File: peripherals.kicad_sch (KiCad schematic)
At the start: 0 parts

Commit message: Initiliase main components
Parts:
- added BZ1: Buzzer, Buzzer_Beeper:Buzzer_CUI_CPT-9019S-SMT, symbol Device:Buzzer
- added J10: Cam 2, S05B_PASK_2_LF__SN_:CONN_S05B-PASK-2_JST, symbol 2025-06-21_05-21-07:S05B-PASK-2LFSN
- added J11: Cam 3, S05B_PASK_2_LF__SN_:CONN_S05B-PASK-2_JST, symbol 2025-06-21_05-21-07:S05B-PASK-2LFSN
- added J12: Encoder, Connector_PinHeader_1.00mm:PinHeader_1x04_P1.00mm_Vertical, symbol Connector:Conn_01x04_Pin
- added J13: Servo, Connector_PinHeader_1.00mm:PinHeader_1x03_P1.00mm_Vertical, symbol Connector:Conn_01x03_Pin
- added J9: Cam 1, S05B_PASK_2_LF__SN_:CONN_S05B-PASK-2_JST, symbol 2025-06-21_05-21-07:S05B-PASK-2LFSN

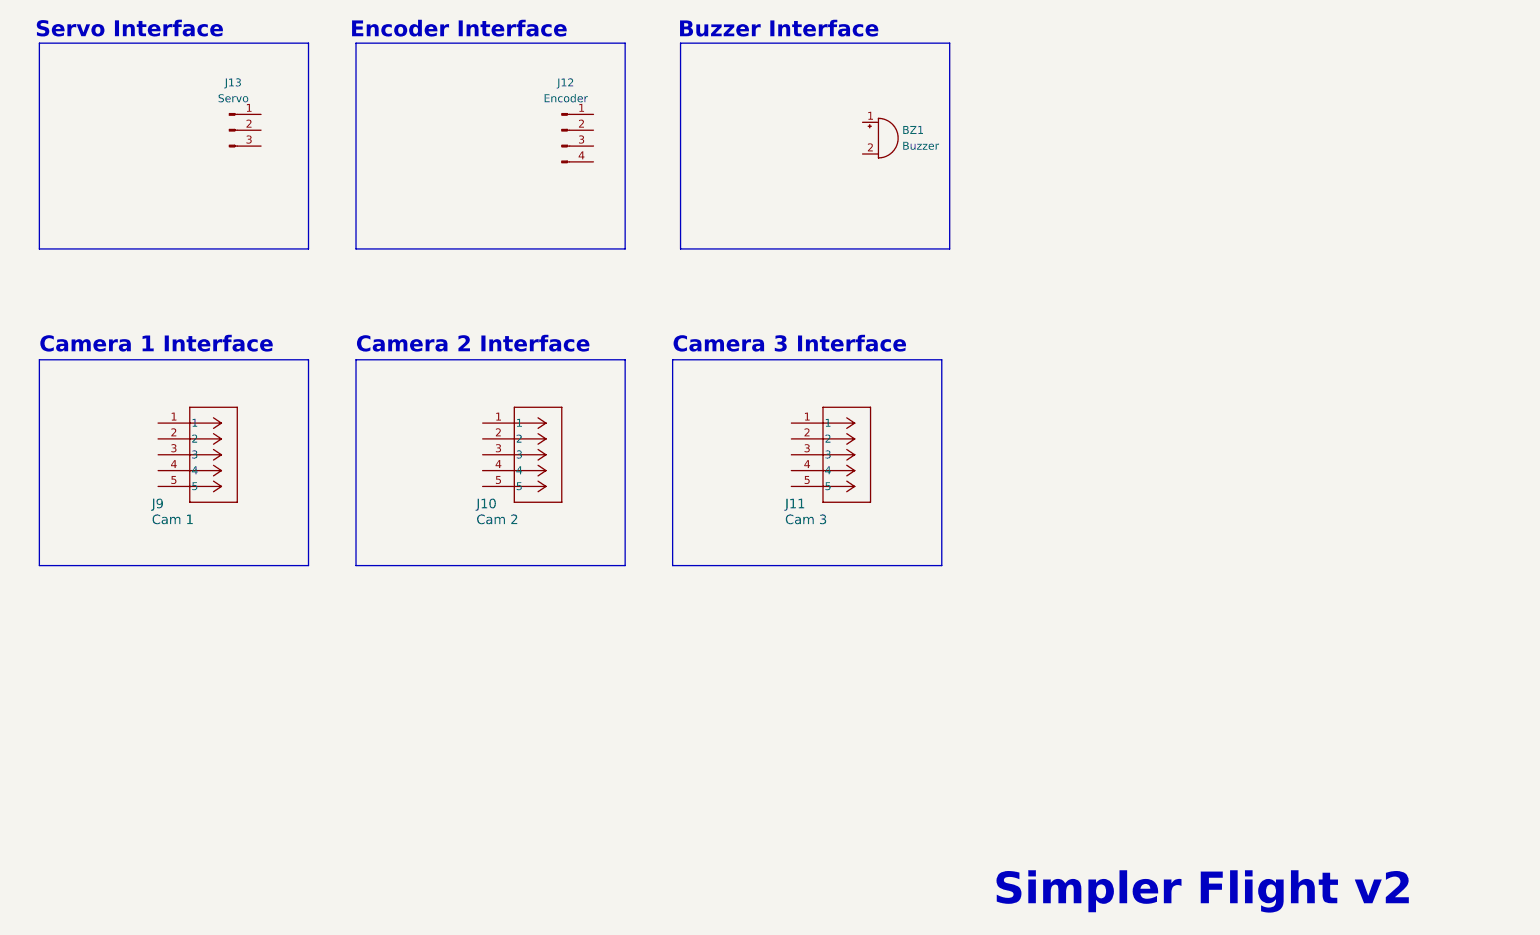
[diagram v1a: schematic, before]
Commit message: Update schematic, pending power sims, updated README
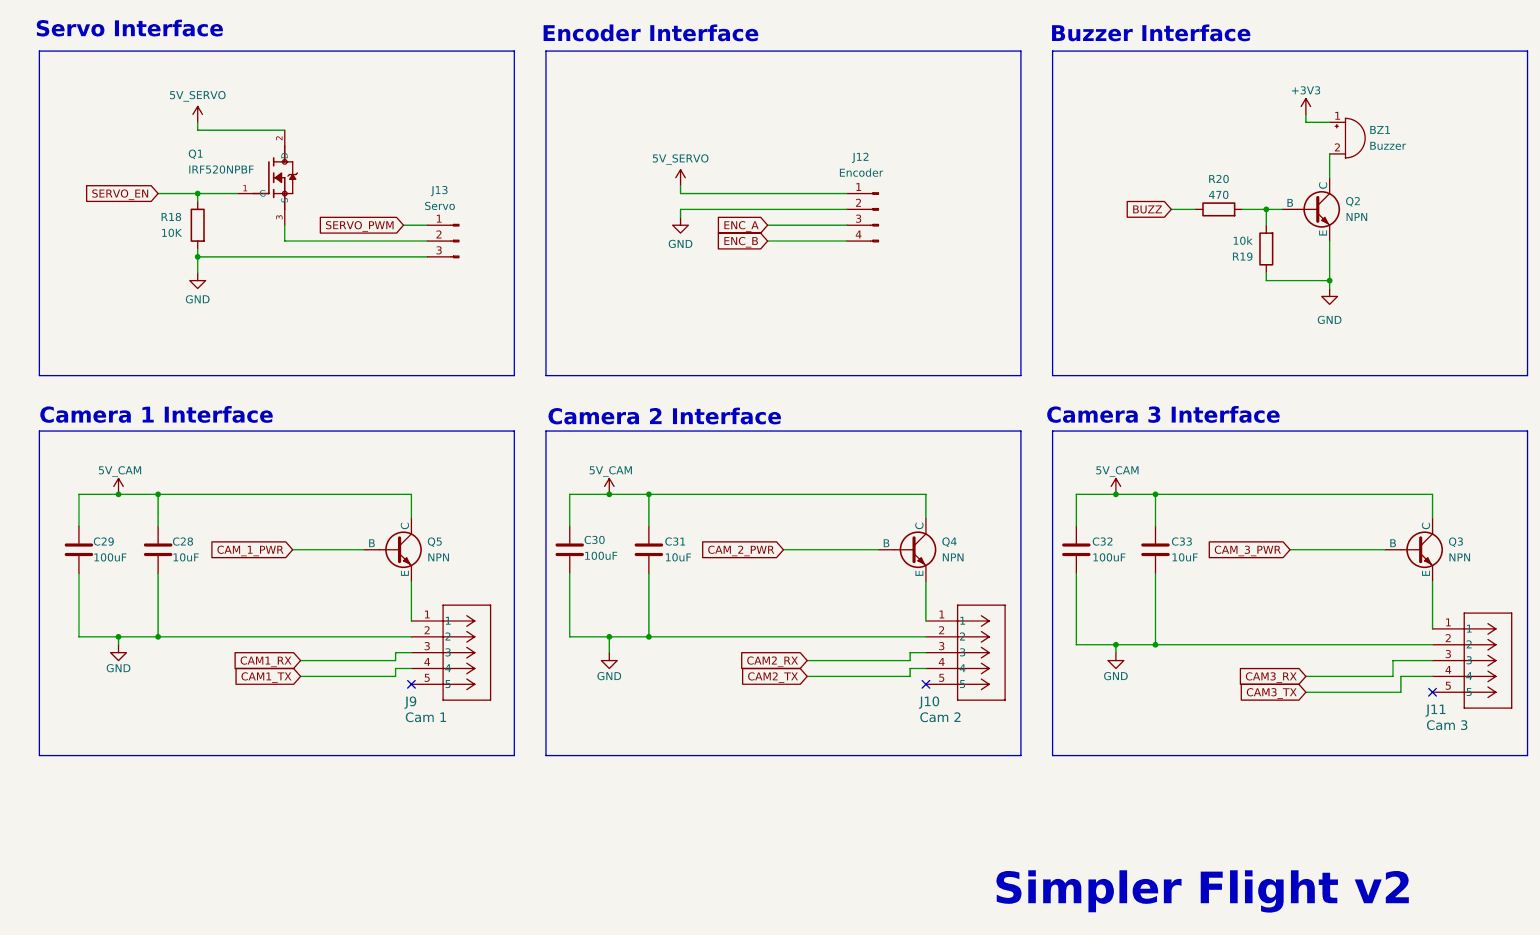
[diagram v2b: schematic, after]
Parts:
- added C28, C31, C33: 10uF, Capacitor_SMD:C_0805_2012Metric_Pad1.18x1.45mm_HandSolder, symbol Device:C
- added C29, C30, C32: 100uF, Capacitor_SMD:C_0805_2012Metric_Pad1.18x1.45mm_HandSolder, symbol Device:C
- added Q1: IRF520NPBF, IRF520NPBF:TO-220-3, symbol IRF520NPBF:IRF520NPBF
- added Q2, Q3, Q4, Q5: NPN, FSB560A:SSOT3_3X1P5_ONS, symbol Simulation_SPICE:NPN
- added R18: 10K, Resistor_SMD:R_0805_2012Metric_Pad1.20x1.40mm_HandSolder, symbol Device:R
- added R19: 10k, Resistor_SMD:R_0805_2012Metric_Pad1.20x1.40mm_HandSolder, symbol Device:R
- added R20: 470, Resistor_SMD:R_0805_2012Metric_Pad1.20x1.40mm_HandSolder, symbol Device:R
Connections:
- net +3V3: now reaches BZ1.1 (+)
- net at BZ1.2 (-): now also Q2.1 (C)
- net at J11.1: now also Q3.3 (E)
- net GND: now reaches J11.2
- net GND: now also J10.2, J12.2 (Pin_2), J13.3 (Pin_3), J9.2, C28.2, C29.2, C30.2, C31.2, C32.2, C33.2, Q2.3 (E), R18.2, R19.1
- net CAM3_RX: now reaches J11.3
- net CAM3_TX: now reaches J11.4
- net at J10.1: now also Q4.3 (E)
- net CAM2_RX: now reaches J10.3
- net CAM2_TX: now reaches J10.4
- net at J9.1: now also Q5.3 (E)
- net CAM1_RX: now reaches J9.3
- net CAM1_TX: now reaches J9.4
- net 5V_SERVO: now reaches J12.1 (Pin_1)
- net 5V_SERVO: now also Q1.2 (D)
- net ENC_A: now reaches J12.3 (Pin_3)
- net ENC_B: now reaches J12.4 (Pin_4)
- net SERVO_PWM: now reaches J13.1 (Pin_1)
- net at J13.2 (Pin_2): now also Q1.3 (S)
- new net: Q2.2 (B), R19.2, R20.2
- new net 5V_CAM: C28.1, C29.1, C30.1, C31.1, C32.1, C33.1, Q3.1 (C), Q4.1 (C), Q5.1 (C)
- new net BUZZ: R20.1
- new net CAM_1_PWR: Q5.2 (B)
- new net CAM_2_PWR: Q4.2 (B)
- new net CAM_3_PWR: Q3.2 (B)
- new net SERVO_EN: Q1.1 (G), R18.1
- no-connect marks 0 -> 3
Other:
- moved on the sheet: BZ1, J10, J11, J12, J13, J9

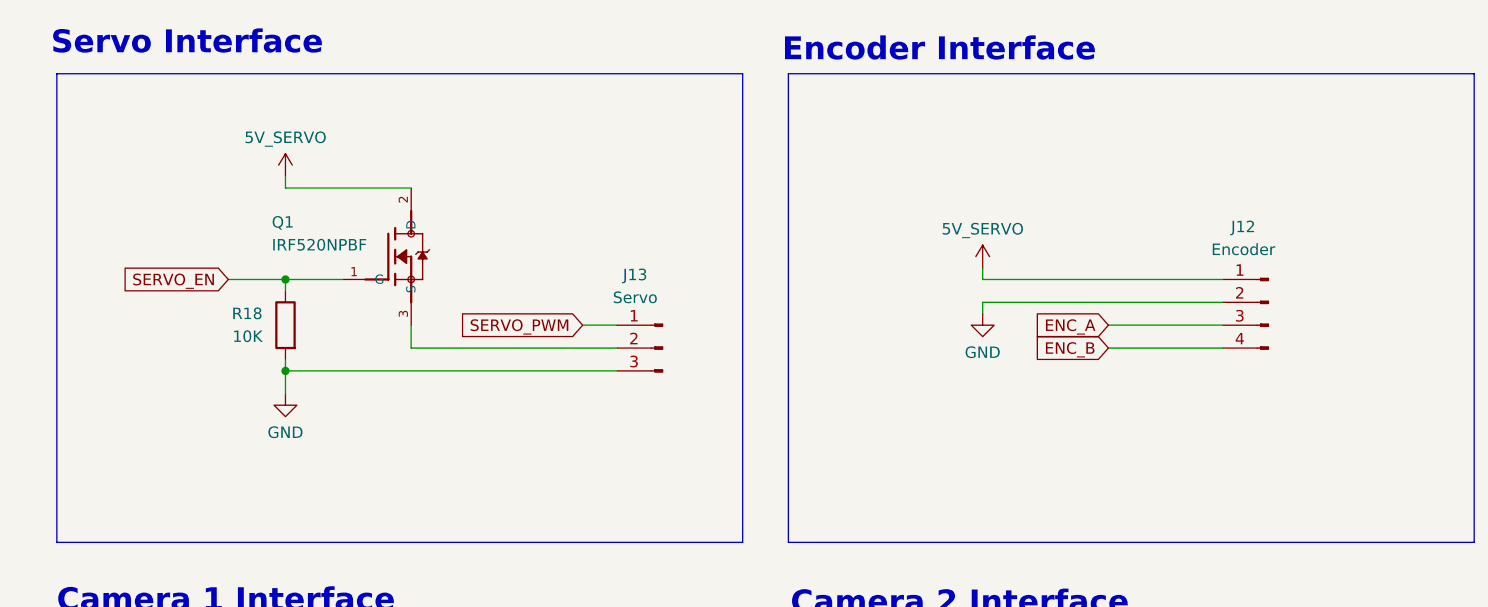
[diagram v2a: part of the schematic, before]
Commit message: Remove transistor enable for servo power. Added falstad sim files
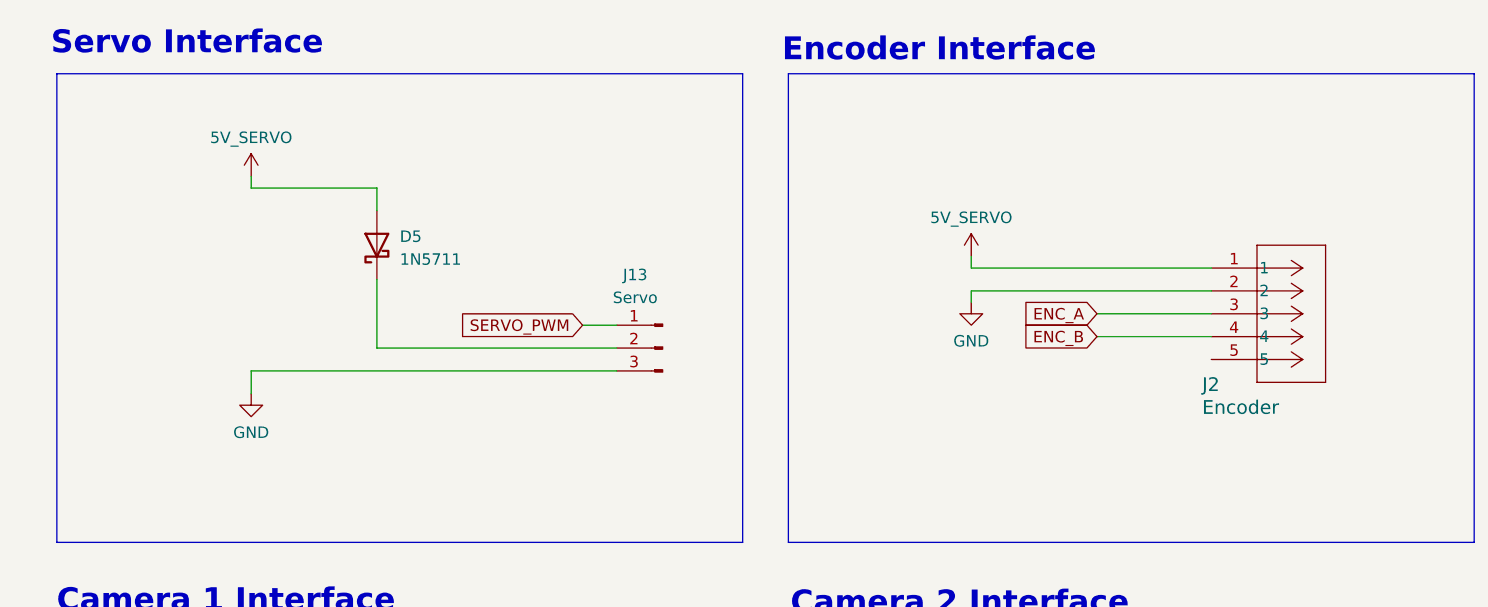
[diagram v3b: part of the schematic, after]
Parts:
- removed J12: Encoder, Connector_PinHeader_1.00mm:PinHeader_1x04_P1.00mm_Vertical, symbol Connector:Conn_01x04_Pin
- removed Q1: IRF520NPBF, IRF520NPBF:TO-220-3, symbol IRF520NPBF:IRF520NPBF
- removed R18: 10K, Resistor_SMD:R_0805_2012Metric_Pad1.20x1.40mm_HandSolder, symbol Device:R
- added D5: 1N5711, Diode_THT:D_DO-35_SOD27_P7.62mm_Horizontal, symbol Diode:1N5711
- added J2: Encoder, S05B_PASK_2_LF__SN_:CONN_S05B-PASK-2_JST, symbol 2025-06-21_05-21-07:S05B-PASK-2LFSN
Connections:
- net 5V_SERVO: now also D5.2 (A), J2.1
- net ENC_A: now also J2.3
- net ENC_B: now also J2.4
- net GND: now also J2.2
- net at J13.2 (Pin_2): now also D5.1 (K)

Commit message: Updated schematics
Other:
- note added: "CAS Board 2025"
- note removed: "Simpler Flight v2"

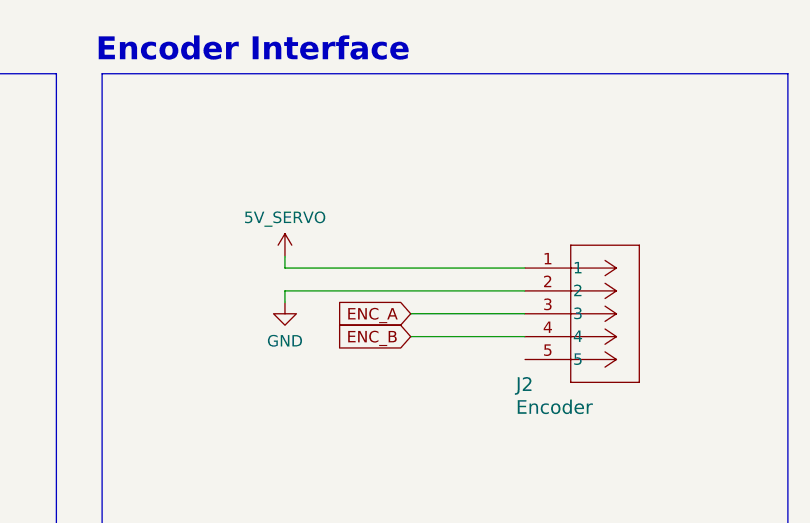
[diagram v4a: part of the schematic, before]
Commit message: added schotkey diode for encoder power
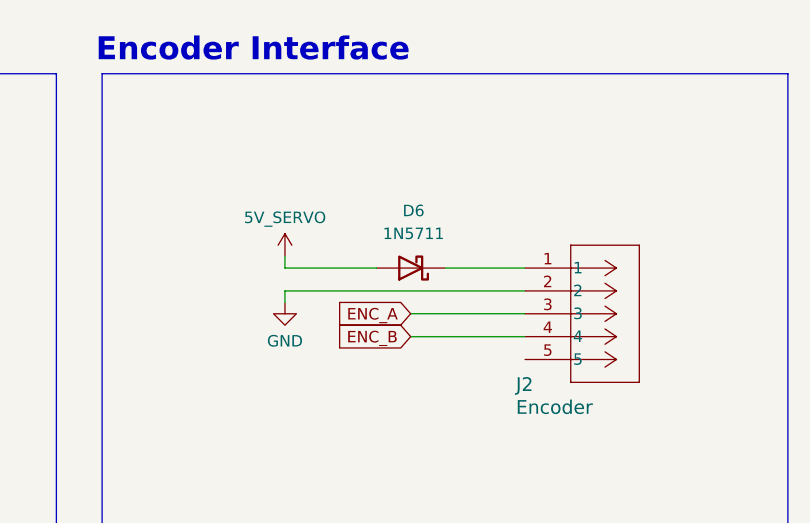
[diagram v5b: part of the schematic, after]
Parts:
- added D6: 1N5711, Diode_THT:D_DO-35_SOD27_P7.62mm_Horizontal, symbol Diode:1N5711
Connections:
- net 5V_SERVO: now also D6.2 (A); no longer J2.1
- new net: D6.1 (K), J2.1
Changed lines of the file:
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@@
 	(wire
 		(pts
+			(xy 144.78 60.96) (xy 153.67 60.96)
+		)
+		(stroke
+			(width 0)
+			(type default)
+		)
+	)
+	(wire
+		(pts
 			(xy 82.55 139.7) (xy 82.55 138.43)
 		)
@@
 	(wire
 		(pts
+			(xy 127 60.96) (xy 137.16 60.96)
+		)
+		(stroke
+			(width 0)
+			(type default)
+		)
+	)
+	(wire
+		(pts
 			(xy 85.09 124.46) (xy 85.09 130.81)
 		)
@@
 		)
 	)
-	(wire
-		(pts
-			(xy 153.67 60.96) (xy 127 60.96)
-		)
-		(stroke
-			(width 0)
-			(type default)
-		)
-	)
 	(polyline
 		(pts
@@
 					(unit 1)
 				)
+			)
+		)
+	)
+	(symbol
+		(lib_id "Diode:1N5711")
+		(at 140.97 60.96 180)
+		(unit 1)
+		(exclude_from_sim no)
+		(in_bom yes)
+		(on_board yes)
+		(dnp no)
+		(fields_autoplaced yes)
+		(property "Reference" "D6"
+			(at 141.2875 54.61 0)
+			(effects
+				(font
+					(size 1.27 1.27)
+				)
+			)
+		)
+		(property "Value" "1N5711"
+			(at 141.2875 57.15 0)
+			(effects
+				(font
+					(size 1.27 1.27)
+				)
+			)
+		)
+		(property "Footprint" "Diode_THT:D_DO-35_SOD27_P7.62mm_Horizontal"
+			(at 140.97 56.515 0)
+			(effects
+				(font
+					(size 1.27 1.27)
+				)
+				(hide yes)
+			)
+		)
+		(property "Datasheet" "https://www.microsemi.com/document-portal/doc_download/8865-lds-0040-datasheet"
+			(at 140.97 60.96 0)
+			(effects
+				(font
+					(size 1.27 1.27)
+				)
+				(hide yes)
+			)
+		)
+		(property "Description" "70V 33mA Schottky diode, DO-35"
+			(at 140.97 60.96 0)
+			(effects
+				(font
+					(size 1.27 1.27)
+				)
+				(hide yes)
+			)
+		)
+		(pin "2"
+		)
+		(pin "1"
+		)
+		(instances
+			(project "SimplerFlight_v2"
+				(path "/05521696-5bcb-4d0e-9e87-bbc993e58ce4/48646a32-6556-4772-9e6c-3c45575ecce9"
+					(reference "D6")
+					(unit 1)
+				)

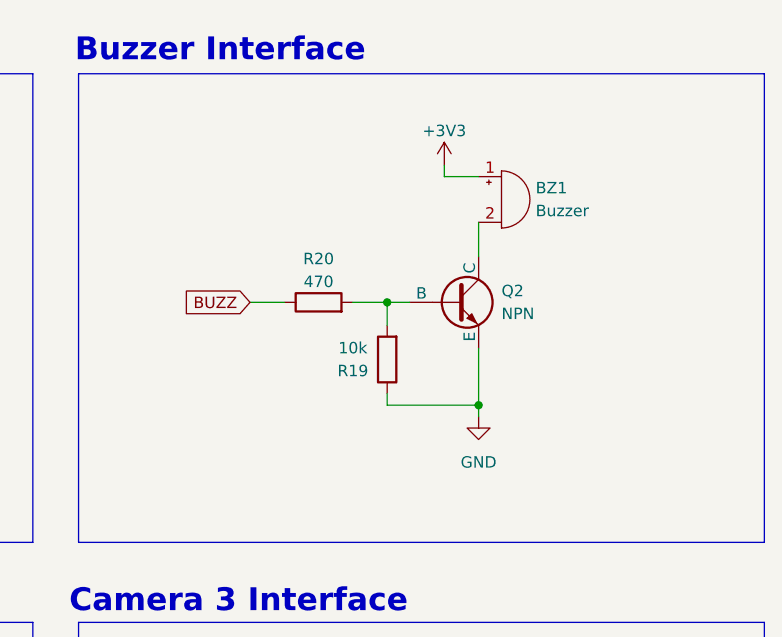
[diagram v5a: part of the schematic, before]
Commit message: Update buzzer circuit and add simulation
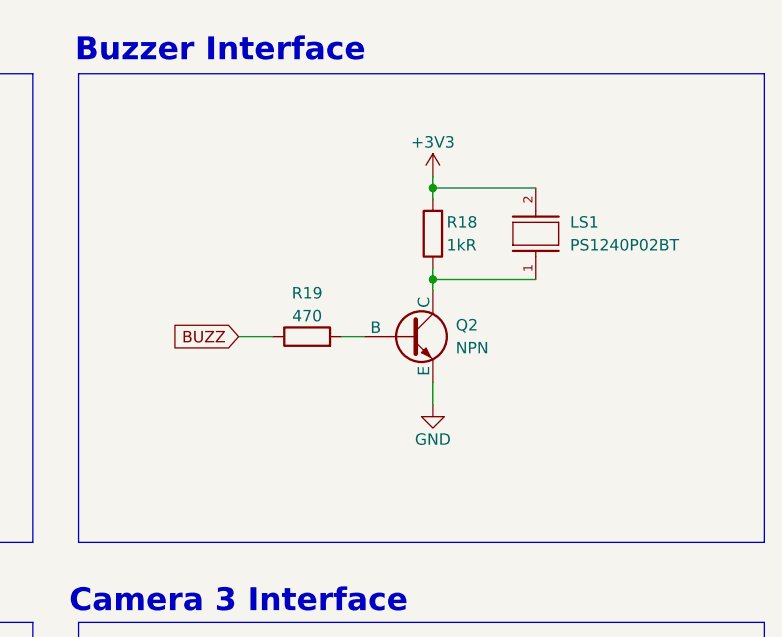
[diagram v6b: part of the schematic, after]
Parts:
- removed BZ1: Buzzer, Buzzer_Beeper:Buzzer_CUI_CPT-9019S-SMT, symbol Device:Buzzer
- removed R20: 470, Resistor_SMD:R_0805_2012Metric_Pad1.20x1.40mm_HandSolder, symbol Device:R
- added LS1: PS1240P02BT, PS1240P02BT:XDCR_PS1240P02BT, symbol PS1240P02BT:PS1240P02BT
- added R18: 1kR, Resistor_SMD:R_0805_2012Metric_Pad1.20x1.40mm_HandSolder, symbol Device:R
- R19: value 10k -> 470
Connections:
- net +3V3: now also LS1.2, R18.2
- net BUZZ: now also R19.1
- net GND: no longer R19.1
- net at Q2.1 (C): now also LS1.1, R18.1
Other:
- moved on the sheet: Q2
